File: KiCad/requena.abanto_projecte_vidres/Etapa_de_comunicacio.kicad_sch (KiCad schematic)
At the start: 10 parts, among them J1 DE9_Pins, J2 DE9_Pins, U1 MAX232, U3 TJA1051TK-3

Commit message: clase
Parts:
- added C5: C_Small, symbol Device:C_Small
- added D1, D2: D, symbol Device:D
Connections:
- net GND: now also C5.2; no longer R1.2, R2.1
- new net: C5.1, R1.2, R2.1
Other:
- note added: "TTL-232R"
- moved on the sheet: J2

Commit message: arreglos :)
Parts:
- removed C1, C2, C3, C4: 1uF, symbol Device:C
- removed U1: MAX232, symbol Interface_UART:MAX232
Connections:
- net UART_RX: now also J1.1
- net UART_TX: now also J1.2
- no-connect marks 15 -> 11
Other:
- moved on the sheet: C5, D1, D2, J1, J2, R1, R2, U3

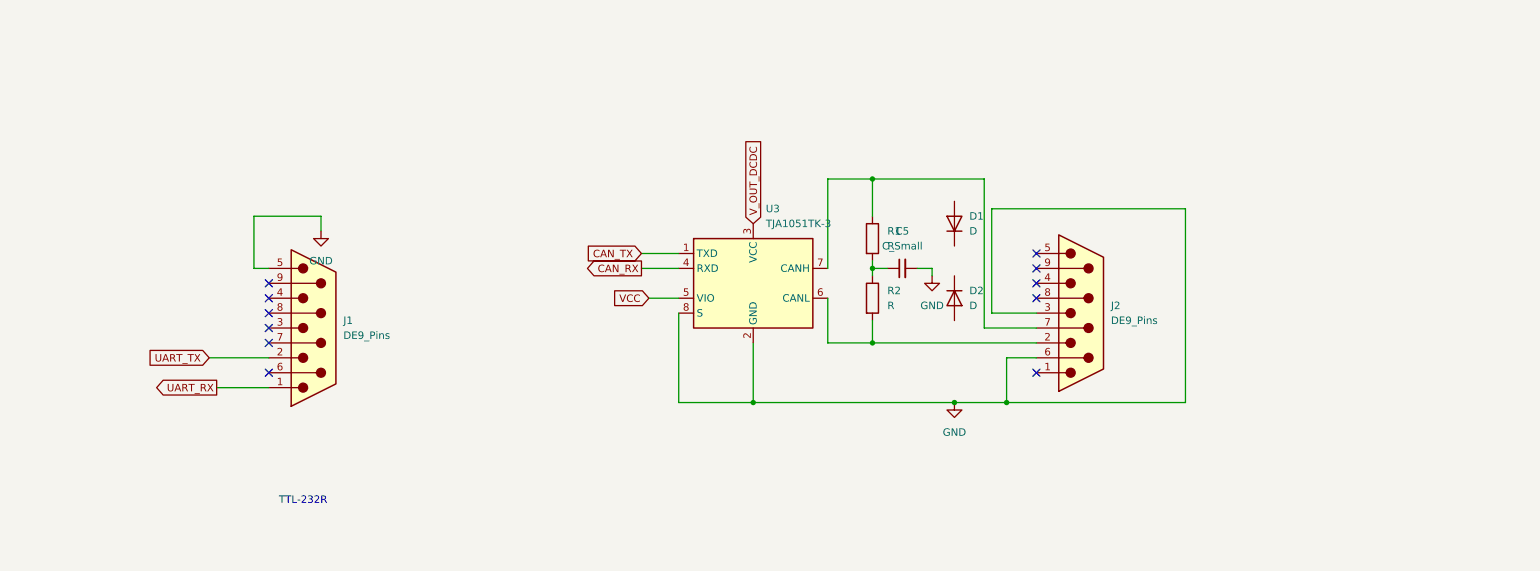
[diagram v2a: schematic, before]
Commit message: millora el esquematic
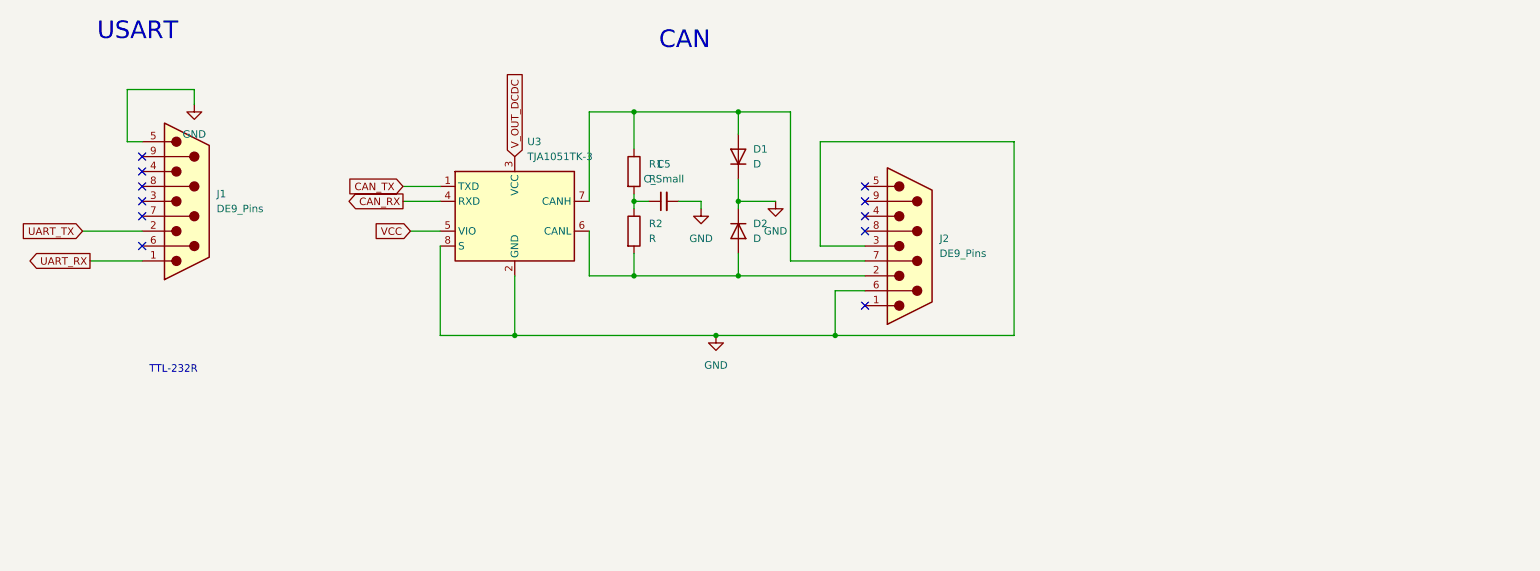
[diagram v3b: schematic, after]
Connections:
- net GND: now also D1.1 (K), D2.1 (K)
- net at J2.2, R2.2, U3.6 (CANL): now also D2.2 (A)
- net at J2.7, R1.1, U3.7 (CANH): now also D1.2 (A)
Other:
- note added: "CAN"
- note added: "USART"
- moved on the sheet: C5, D1, D2, J1, J2, R1, R2, U3
